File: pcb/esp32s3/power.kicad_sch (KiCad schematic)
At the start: 15 parts, among them J1 USB_C_Receptacle_USB2.0_14P, J2 Battery, Q1 DMG3414U, U2 AZ1117-3.3, U3 MCP73831-2-OT, U4 USBLC6-2SC6

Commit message: updated footprints / schematic
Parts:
- C13, C14: footprint (none) -> Capacitor_SMD:C_0402_1005Metric
- J1: footprint (none) -> Connector_USB:USB_C_Receptacle_G-Switch_GT-USB-7010ASV
- R10: renamed from R9; footprint (none) -> Resistor_SMD:R_0402_1005Metric
- R11: renamed from R10; footprint (none) -> Resistor_SMD:R_0402_1005Metric
- R6, R7: footprint (none) -> Resistor_SMD:R_0402_1005Metric
- R8: renamed from R5; footprint (none) -> Resistor_SMD:R_0402_1005Metric
- R9: renamed from R4; footprint (none) -> Resistor_SMD:R_0402_1005Metric
- U2: footprint (none) -> Package_TO_SOT_SMD:SOT-223-3_TabPin2
- renumbered U4 to U3, U3 to U4
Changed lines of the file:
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@@
 		(dnp no)
 		(fields_autoplaced yes)
-		(property "Reference" "#PWR017"
+		(property "Reference" "#PWR027"
 			(at 229.87 29.21 0)
 			(effects
@@
 			(project "esp32s3"
 				(path "/834edf73-57a5-43b4-ab36-0b077e93e6d5/ae5309e0-349d-45c3-b1b4-6edffcac73ca"
-					(reference "#PWR017")
+					(reference "#PWR027")
 					(unit 1)
 				)
@@
 		(on_board yes)
 		(dnp no)
-		(property "Reference" "U4"
+		(property "Reference" "U3"
 			(at 89.154 103.378 0)
 			(effects
@@
 			(project "esp32s3"
 				(path "/834edf73-57a5-43b4-ab36-0b077e93e6d5/ae5309e0-349d-45c3-b1b4-6edffcac73ca"
-					(reference "U4")
+					(reference "U3")
 					(unit 1)
 				)
@@
 		(on_board yes)
 		(dnp no)
-		(property "Reference" "#PWR023"
+		(property "Reference" "#PWR026"
 			(at 148.59 31.75 0)
 			(effects
@@
 			(project "esp32s3"
 				(path "/834edf73-57a5-43b4-ab36-0b077e93e6d5/ae5309e0-349d-45c3-b1b4-6edffcac73ca"
-					(reference "#PWR023")
+					(reference "#PWR026")
 					(unit 1)
 				)
@@
 		(on_board yes)
 		(dnp no)
-		(property "Reference" "R10"
+		(property "Reference" "R11"
 			(at 238.76 146.304 0)
 			(effects
@@
 			)
 		)
-		(property "Footprint" ""
+		(property "Footprint" "Resistor_SMD:R_0402_1005Metric"
 			(at 240.284 138.684 90)
 			(effects
@@
 			(project "esp32s3"
 				(path "/834edf73-57a5-43b4-ab36-0b077e93e6d5/ae5309e0-349d-45c3-b1b4-6edffcac73ca"
-					(reference "R10")
+					(reference "R11")
 					(unit 1)
 				)
@@
 		(on_board yes)
 		(dnp no)
-		(property "Reference" "R5"
+		(property "Reference" "R8"
 			(at 121.412 40.64 0)
 			(effects
@@
 			)
 		)
-		(property "Footprint" ""
+		(property "Footprint" "Resistor_SMD:R_0402_1005Metric"
 			(at 129.286 42.164 90)
 			(effects
@@
 			(project "esp32s3"
 				(path "/834edf73-57a5-43b4-ab36-0b077e93e6d5/ae5309e0-349d-45c3-b1b4-6edffcac73ca"
-					(reference "R5")
+					(reference "R8")
 					(unit 1)
 				)
@@
 		(dnp no)
 		(fields_autoplaced yes)
-		(property "Reference" "#PWR022"
+		(property "Reference" "#PWR025"
 			(at 138.43 55.88 0)
 			(effects
@@
 			(project "esp32s3"
 				(path "/834edf73-57a5-43b4-ab36-0b077e93e6d5/ae5309e0-349d-45c3-b1b4-6edffcac73ca"
-					(reference "#PWR022")
+					(reference "#PWR025")
 					(unit 1)
 				)
@@
 		(dnp no)
 		(fields_autoplaced yes)
-		(property "Reference" "#PWR027"
+		(property "Reference" "#PWR023"
 			(at 85.09 127 0)
 			(effects
@@
 			(project "esp32s3"
 				(path "/834edf73-57a5-43b4-ab36-0b077e93e6d5/ae5309e0-349d-45c3-b1b4-6edffcac73ca"
-					(reference "#PWR027")
+					(reference "#PWR023")
 					(unit 1)
 				)
@@
 		(on_board yes)
 		(dnp no)
-		(property "Reference" "#PWR019"
+		(property "Reference" "#PWR028"
 			(at 229.87 58.42 0)
 			(effects
@@
 			(project "esp32s3"
 				(path "/834edf73-57a5-43b4-ab36-0b077e93e6d5/ae5309e0-349d-45c3-b1b4-6edffcac73ca"
-					(reference "#PWR019")
+					(reference "#PWR028")
 					(unit 1)
 				)
@@
 		(on_board yes)
 		(dnp no)
-		(property "Reference" "#PWR028"
+		(property "Reference" "#PWR021"
 			(at 80.01 109.22 0)
 			(effects
@@
 			(project "esp32s3"
 				(path "/834edf73-57a5-43b4-ab36-0b077e93e6d5/ae5309e0-349d-45c3-b1b4-6edffcac73ca"
-					(reference "#PWR028")
+					(reference "#PWR021")
 					(unit 1)
 				)
@@
 		(dnp no)
 		(fields_autoplaced yes)
-		(property "Reference" "#PWR029"
+		(property "Reference" "#PWR030"
 			(at 240.03 85.09 0)
 			(effects
@@
 			(project "esp32s3"
 				(path "/834edf73-57a5-43b4-ab36-0b077e93e6d5/ae5309e0-349d-45c3-b1b4-6edffcac73ca"
-					(reference "#PWR029")
+					(reference "#PWR030")
 					(unit 1)
 				)
@@
 		(dnp no)
 		(fields_autoplaced yes)
-		(property "Reference" "#PWR030"
+		(property "Reference" "#PWR031"
 			(at 240.03 95.25 0)
 			(effects
@@
 			(project "esp32s3"
 				(path "/834edf73-57a5-43b4-ab36-0b077e93e6d5/ae5309e0-349d-45c3-b1b4-6edffcac73ca"
-					(reference "#PWR030")
+					(reference "#PWR031")
 					(unit 1)
 				)
@@
 		(dnp no)
 		(fields_autoplaced yes)
-		(property "Reference" "#PWR040"
+		(property "Reference" "#PWR029"
 			(at 233.68 130.81 0)
 			(effects
@@
 			(project "esp32s3"
 				(path "/834edf73-57a5-43b4-ab36-0b077e93e6d5/ae5309e0-349d-45c3-b1b4-6edffcac73ca"
-					(reference "#PWR040")
+					(reference "#PWR029")
 					(unit 1)
 				)
@@
 		(dnp no)
 		(fields_autoplaced yes)
-		(property "Reference" "#PWR041"
+		(property "Reference" "#PWR032"
 			(at 247.65 146.05 0)
 			(effects
@@
 			(project "esp32s3"
 				(path "/834edf73-57a5-43b4-ab36-0b077e93e6d5/ae5309e0-349d-45c3-b1b4-6edffcac73ca"
-					(reference "#PWR041")
+					(reference "#PWR032")
 					(unit 1)
 				)
@@
 			)
 		)
-		(property "Footprint" ""
+		(property "Footprint" "Resistor_SMD:R_0402_1005Metric"
 			(at 87.376 92.964 90)
 			(effects
@@
 		(dnp no)
 		(fields_autoplaced yes)
-		(property "Reference" "#PWR025"
+		(property "Reference" "#PWR018"
 			(at 52.07 132.08 0)
 			(effects
@@
 			(project "esp32s3"
 				(path "/834edf73-57a5-43b4-ab36-0b077e93e6d5/ae5309e0-349d-45c3-b1b4-6edffcac73ca"
-					(reference "#PWR025")
+					(reference "#PWR018")
 					(unit 1)
 				)
@@
 		(dnp no)
 		(fields_autoplaced yes)
-		(property "Reference" "#PWR016"
+		(property "Reference" "#PWR019"
 			(at 60.96 33.02 0)
 			(effects
@@
 			(project "esp32s3"
 				(path "/834edf73-57a5-43b4-ab36-0b077e93e6d5/ae5309e0-349d-45c3-b1b4-6edffcac73ca"
-					(reference "#PWR016")
+					(reference "#PWR019")
 					(unit 1)
 				)
@@
 			)
 		)
-		(property "Footprint" ""
+		(property "Footprint" "Capacitor_SMD:C_0402_1005Metric"
 			(at 58.1152 38.1 0)
 			(effects
@@
 		(on_board yes)
 		(dnp no)
-		(property "Reference" "R9"
+		(property "Reference" "R10"
 			(at 227.076 132.08 0)
 			(effects
@@
 			)
 		)
-		(property "Footprint" ""
+		(property "Footprint" "Resistor_SMD:R_0402_1005Metric"
 			(at 234.696 133.604 90)
 			(effects
@@
 			(project "esp32s3"
 				(path "/834edf73-57a5-43b4-ab36-0b077e93e6d5/ae5309e0-349d-45c3-b1b4-6edffcac73ca"
-					(reference "R9")
+					(reference "R10")
 					(unit 1)
 				)
@@
 		(dnp no)
 		(fields_autoplaced yes)
-		(property "Reference" "#PWR026"
+		(property "Reference" "#PWR020"
 			(at 73.66 85.09 0)
 			(effects
@@
 			(project "esp32s3"
 				(path "/834edf73-57a5-43b4-ab36-0b077e93e6d5/ae5309e0-349d-45c3-b1b4-6edffcac73ca"
-					(reference "#PWR026")
+					(reference "#PWR020")
 					(unit 1)
 				)
@@
 			)
 		)
-		(property "Footprint" ""
+		(property "Footprint" "Capacitor_SMD:C_0402_1005Metric"
 			(at 33.9852 38.1 0)
 			(effects
@@
 		(dnp no)
 		(fields_autoplaced yes)
-		(property "Reference" "#PWR015"
+		(property "Reference" "#PWR017"
 			(at 45.72 48.26 0)
 			(effects
@@
 			(project "esp32s3"
 				(path "/834edf73-57a5-43b4-ab36-0b077e93e6d5/ae5309e0-349d-45c3-b1b4-6edffcac73ca"
-					(reference "#PWR015")
+					(reference "#PWR017")
 					(unit 1)
 				)
@@
 			)
 		)
-		(property "Footprint" ""
+		(property "Footprint" "Connector_USB:USB_C_Receptacle_G-Switch_GT-USB-7010ASV"
 			(at 55.88 99.06 0)
 			(effects
@@
 		(dnp no)
 		(fields_autoplaced yes)
-		(property "Reference" "#PWR020"
+		(property "Reference" "#PWR034"
 			(at 255.27 44.45 0)
 			(effects
@@
 			(project "esp32s3"
 				(path "/834edf73-57a5-43b4-ab36-0b077e93e6d5/ae5309e0-349d-45c3-b1b4-6edffcac73ca"
-					(reference "#PWR020")
+					(reference "#PWR034")
 					(unit 1)
 				)
@@
 		(on_board yes)
 		(dnp no)
-		(property "Reference" "#PWR024"
+		(property "Reference" "#PWR022"
 			(at 83.82 104.14 0)
 			(effects
@@
 			(project "esp32s3"
 				(path "/834edf73-57a5-43b4-ab36-0b077e93e6d5/ae5309e0-349d-45c3-b1b4-6edffcac73ca"
-					(reference "#PWR024")
+					(reference "#PWR022")
 					(unit 1)
 				)
@@
 		(dnp no)
 		(fields_autoplaced yes)
-		(property "Reference" "R4"
+		(property "Reference" "R9"
 			(at 232.41 44.4499 0)
 			(effects
@@
 			)
 		)
-		(property "Footprint" ""
+		(property "Footprint" "Resistor_SMD:R_0402_1005Metric"
 			(at 230.886 45.974 90)
 			(effects
@@
 			(project "esp32s3"
 				(path "/834edf73-57a5-43b4-ab36-0b077e93e6d5/ae5309e0-349d-45c3-b1b4-6edffcac73ca"
-					(reference "R4")
+					(reference "R9")
 					(unit 1)
 				)
@@
 		(dnp no)
 		(fields_autoplaced yes)
-		(property "Reference" "#PWR021"
+		(property "Reference" "#PWR024"
 			(at 138.43 25.4 0)
 			(effects
@@
 			(project "esp32s3"
 				(path "/834edf73-57a5-43b4-ab36-0b077e93e6d5/ae5309e0-349d-45c3-b1b4-6edffcac73ca"
-					(reference "#PWR021")
+					(reference "#PWR024")
 					(unit 1)
 				)
@@
 		(dnp no)
 		(fields_autoplaced yes)
-		(property "Reference" "#PWR018"
+		(property "Reference" "#PWR033"
 			(at 248.92 25.4 0)
 			(effects
@@
 			(project "esp32s3"
 				(path "/834edf73-57a5-43b4-ab36-0b077e93e6d5/ae5309e0-349d-45c3-b1b4-6edffcac73ca"
-					(reference "#PWR018")
+					(reference "#PWR033")
 					(unit 1)
 				)
@@
 		(dnp no)
 		(fields_autoplaced yes)
-		(property "Reference" "#PWR014"
+		(property "Reference" "#PWR016"
 			(at 29.21 33.02 0)
 			(effects
@@
 			(project "esp32s3"
 				(path "/834edf73-57a5-43b4-ab36-0b077e93e6d5/ae5309e0-349d-45c3-b1b4-6edffcac73ca"
-					(reference "#PWR014")
+					(reference "#PWR016")
 					(unit 1)
 				)
@@
 		(on_board yes)
 		(dnp no)
-		(property "Reference" "U3"
+		(property "Reference" "U4"
 			(at 140.97 25.4 0)
 			(effects
@@
 			(project "esp32s3"
 				(path "/834edf73-57a5-43b4-ab36-0b077e93e6d5/ae5309e0-349d-45c3-b1b4-6edffcac73ca"
-					(reference "U3")
+					(reference "U4")
 					(unit 1)
 				)
@@
 			)
 		)
-		(property "Footprint" ""
+		(property "Footprint" "Resistor_SMD:R_0402_1005Metric"
 			(at 82.296 92.964 90)
 			(effects
@@
 			)
 		)
-		(property "Footprint" ""
+		(property "Footprint" "Package_TO_SOT_SMD:SOT-223-3_TabPin2"
 			(at 45.72 24.13 0)
 			(effects

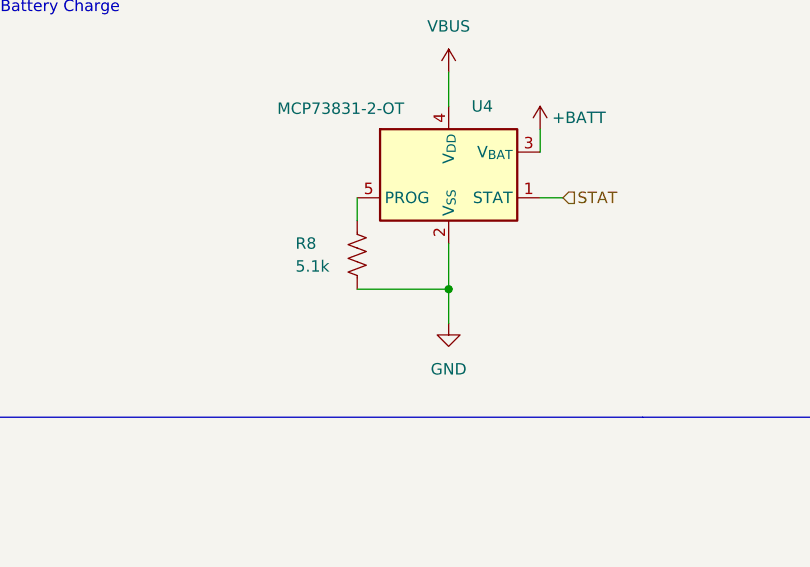
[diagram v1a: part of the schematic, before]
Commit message: Update PCB with new components and footprints
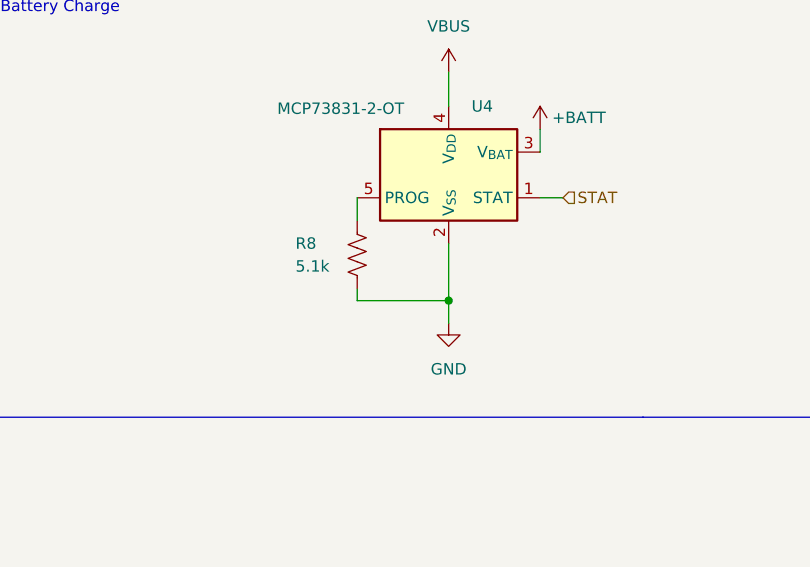
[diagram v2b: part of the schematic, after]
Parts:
- J2: footprint footprints:2 Wire Pads -> custom_comps:2 Wire Pads
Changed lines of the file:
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@@
+	)
+	(junction
+		(at 138.43 46.99)
+		(diameter 0)
+		(color 0 0 0 0)
 	)
 	(junction
@@
 	)
 	(junction
-		(at 138.43 45.72)
-		(diameter 0)
-		(color 0 0 0 0)
-	)
-	(junction
 		(at 83.82 96.52)
 		(diameter 0)
@@
 	(wire
 		(pts
-			(xy 138.43 40.64) (xy 138.43 45.72)
-		)
-		(stroke
-			(width 0)
-			(type default)
-		)
-	)
-	(wire
-		(pts
 			(xy 68.58 113.03) (xy 68.58 102.87)
 		)
@@
 	(wire
 		(pts
+			(xy 138.43 46.99) (xy 138.43 49.53)
+		)
+		(stroke
+			(width 0)
+			(type default)
+		)
+	)
+	(wire
+		(pts
 			(xy 45.72 38.1) (xy 57.15 38.1)
 		)
@@
 	(wire
 		(pts
-			(xy 138.43 45.72) (xy 138.43 49.53)
+			(xy 138.43 40.64) (xy 138.43 46.99)
 		)
 		(stroke
@@
 	(wire
 		(pts
+			(xy 128.27 46.99) (xy 128.27 45.72)
+		)
+		(stroke
+			(width 0)
+			(type default)
+		)
+	)
+	(wire
+		(pts
 			(xy 233.68 127) (xy 233.68 129.54)
 		)
@@
 	(wire
 		(pts
-			(xy 128.27 45.72) (xy 138.43 45.72)
+			(xy 128.27 46.99) (xy 138.43 46.99)
 		)
 		(stroke
@@
 			)
 		)
-		(property "Footprint" "footprints:2 Wire Pads"
+		(property "Footprint" "custom_comps:2 Wire Pads"
 			(at 229.87 83.82 0)
 			(effects

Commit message: pcb kinda almost done!
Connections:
- net USB_D+: now also U3.1 (I/O1); no longer U3.3 (I/O2)
- net USB_D-: now also U3.3 (I/O2); no longer U3.1 (I/O1)
- net at J1.A6 (D+), J1.B6 (D+): now also U3.6 (I/O1); no longer U3.4 (I/O2)
- net at J1.A7 (D-), J1.B7 (D-): now also U3.4 (I/O2); no longer U3.6 (I/O1)
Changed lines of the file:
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@@
 	(wire
 		(pts
-			(xy 80.01 110.49) (xy 71.12 110.49)
+			(xy 68.58 110.49) (xy 80.01 110.49)
 		)
 		(stroke
@@
 	(wire
 		(pts
-			(xy 71.12 110.49) (xy 71.12 97.79)
+			(xy 71.12 97.79) (xy 71.12 113.03)
 		)
 		(stroke
@@
 	(wire
 		(pts
-			(xy 68.58 113.03) (xy 68.58 102.87)
-		)
-		(stroke
-			(width 0)
-			(type default)
-		)
-	)
-	(wire
-		(pts
 			(xy 138.43 21.59) (xy 138.43 25.4)
 		)
@@
 	(wire
 		(pts
+			(xy 90.17 110.49) (xy 95.25 110.49)
+		)
+		(stroke
+			(width 0)
+			(type default)
+		)
+	)
+	(wire
+		(pts
 			(xy 69.85 87.63) (xy 86.36 87.63)
 		)
@@
 	(wire
 		(pts
+			(xy 68.58 102.87) (xy 68.58 110.49)
+		)
+		(stroke
+			(width 0)
+			(type default)
+		)
+	)
+	(wire
+		(pts
 			(xy 229.87 40.64) (xy 234.95 40.64)
 		)
@@
 	(wire
 		(pts
-			(xy 90.17 110.49) (xy 96.52 110.49)
-		)
-		(stroke
-			(width 0)
-			(type default)
-		)
-	)
-	(wire
-		(pts
 			(xy 67.31 102.87) (xy 67.31 104.14)
 		)
@@
 	(wire
 		(pts
+			(xy 71.12 113.03) (xy 80.01 113.03)
+		)
+		(stroke
+			(width 0)
+			(type default)
+		)
+	)
+	(wire
+		(pts
 			(xy 233.68 139.7) (xy 236.22 139.7)
 		)
@@
 	(wire
 		(pts
+			(xy 95.25 113.03) (xy 90.17 113.03)
+		)
+		(stroke
+			(width 0)
+			(type default)
+		)
+	)
+	(wire
+		(pts
 			(xy 128.27 46.99) (xy 138.43 46.99)
 		)
@@
 	(wire
 		(pts
-			(xy 90.17 113.03) (xy 96.52 113.03)
-		)
-		(stroke
-			(width 0)
-			(type default)
-		)
-	)
-	(wire
-		(pts
 			(xy 29.21 29.21) (xy 29.21 30.48)
-		)
-		(stroke
-			(width 0)
-			(type default)
-		)
-	)
-	(wire
-		(pts
-			(xy 80.01 113.03) (xy 68.58 113.03)
 		)
 		(stroke
@@
 	(hierarchical_label "USB_D-"
 		(shape bidirectional)
-		(at 96.52 110.49 0)
+		(at 95.25 113.03 0)
 		(fields_autoplaced yes)
 		(effects
@@
 	(hierarchical_label "USB_D+"
 		(shape bidirectional)
-		(at 96.52 113.03 0)
+		(at 95.25 110.49 0)
 		(fields_autoplaced yes)
 		(effects
